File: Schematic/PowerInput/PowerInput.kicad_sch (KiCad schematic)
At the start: 25 parts, among them J101 PSU1 Pri, J102 PSU2 Pri, J103 PSU1 Sec, J104 PSU2 Sec, J105 Power LED, J106 230VAC In, J107 Power switch, J108 To MainBoard, J109 To Heater PSU

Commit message: Added filtering on PSU1 secondary
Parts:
- added C102: 220µF 35V, Capacitor_THT:CP_Radial_D10.0mm_P7.50mm, symbol Device:C_Polarized
- added FB101, FB102: FerriteBead, Inductor_SMD:L_1812_4532Metric_Pad1.30x3.40mm_HandSolder, symbol Device:FerriteBead
- added L101: 330µH 3.3A, Inductor_THT:L_Radial_D24.4mm_P23.70mm_Murata_1400series, symbol Device:L_Ferrite
- R102: value 1kΩ 1/2W -> 3.9kΩ 1/2W
- renumbered F102 to F101, F101 to F102, J108 to J104, J106 to J105, J105 to J106, J104 to J108
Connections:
- net Earth: now also J103.1 (Pin_1), J104.1 (Pin_1), C102.2; no longer J103.2 (Pin_2), J104.2 (Pin_2)
- net PSU1_19V: now also F101.2, J103.2 (Pin_2); no longer F101.1, J104.1 (Pin_1), R101.1, R102.1
- net PSU2_0V: now also FB102.1; no longer D102.1 (K), J109.2 (Pin_2)
- net PSU2_19V: now also F103.2, J108.1 (Pin_1); no longer F103.1, J109.1 (Pin_1), R103.1
- new net: F101.1, L101.2
- new net: F103.1, FB101.1
- new net HeaterPSU_0V: D102.1 (K), FB102.2, J109.2 (Pin_2)
- new net HeaterPSU_19V: FB101.2, J109.1 (Pin_1), R103.1
- new net MainBoard_19V: C102.1, J104.2 (Pin_2), L101.1, R101.1, R102.1
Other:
- moved on the sheet: D101, D102, F101, F103, J104, J106, J108, J109, R101, R102, R103

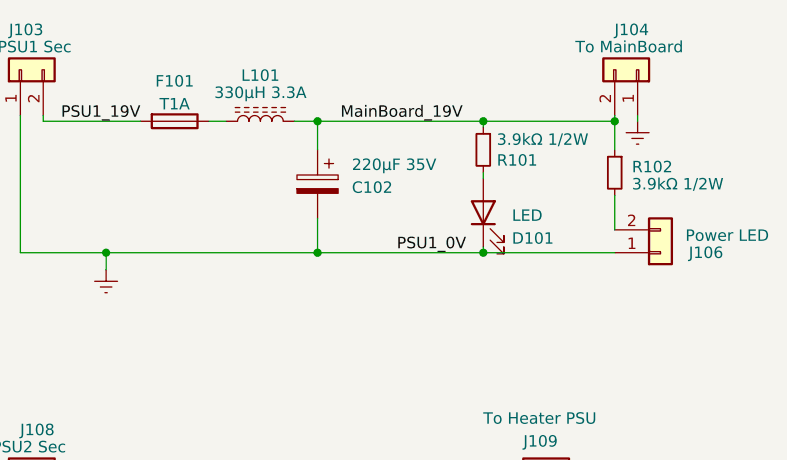
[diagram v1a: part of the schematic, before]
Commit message: Larger mounting hole for rotary switch
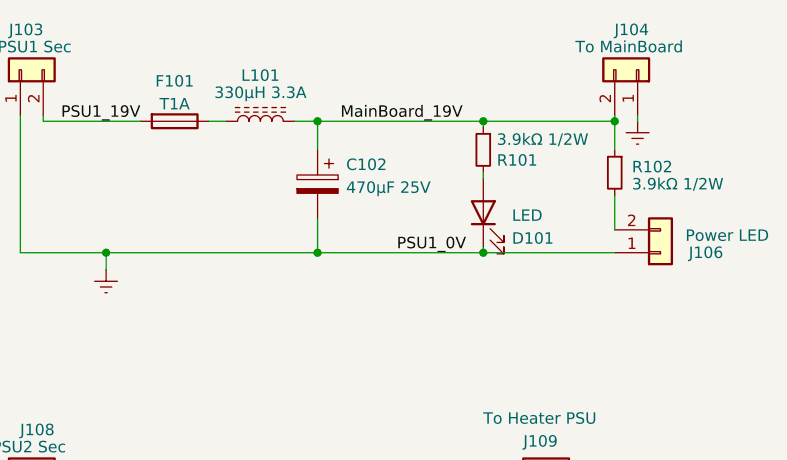
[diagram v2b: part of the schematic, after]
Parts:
- C102: value 220µF 35V -> 470µF 25V
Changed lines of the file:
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@@
   (symbol (lib_id "Device:C_Polarized") (at 172.085 74.93 0) (mirror y) (unit 1)
     (in_bom yes) (on_board yes) (fields_autoplaced)
-    (property "Reference" "C102" (id 0) (at 175.895 75.3111 0)
+    (property "Reference" "C102" (id 0) (at 175.26 72.7709 0)
       (effects (font (size 1.27 1.27)) (justify right))
     )
-    (property "Value" "220µF 35V" (id 1) (at 175.895 72.7711 0)
+    (property "Value" "470µF 25V" (id 1) (at 175.26 75.3109 0)
       (effects (font (size 1.27 1.27)) (justify right))
     )
@@
     )
     (path "/e68d4bfc-28fa-42c7-b027-c6bcd125d5f6"
-      (reference "C102") (unit 1) (value "220µF 35V") (footprint "Capacitor_THT:CP_Radial_D10.0mm_P7.50mm")
+      (reference "C102") (unit 1) (value "470µF 25V") (footprint "Capacitor_THT:CP_Radial_D10.0mm_P7.50mm")
     )
     (path "/089898c7-9db1-4682-8c8f-00decb94c3b6"

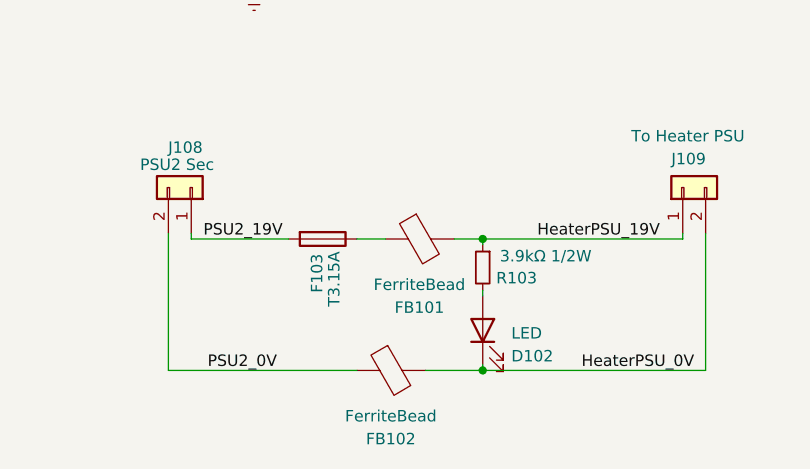
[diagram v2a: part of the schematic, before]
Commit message: Added BOM (bill of materials)
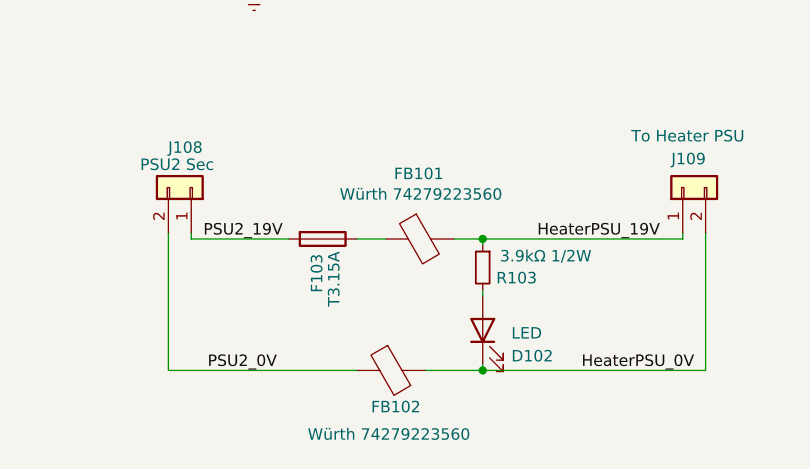
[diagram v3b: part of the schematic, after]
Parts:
- FB101, FB102: value FerriteBead -> Würth 74279223560
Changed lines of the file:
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@@
       (effects (font (size 1.27 1.27)) hide)
     )
-    (property "Datasheet" "~" (id 3) (at 113.03 62.23 0)
+    (property "Datasheet" "https://datasheet.lcsc.com/lcsc/2301061509_DIBO-DB128L-5-08-2P-BK-S_C430601.pdf" (id 3) (at 113.03 62.23 0)
       (effects (font (size 1.27 1.27)) hide)
     )
@@
       (effects (font (size 1.27 1.27)) hide)
     )
-    (property "Datasheet" "~" (id 3) (at 123.19 62.23 0)
+    (property "Datasheet" "https://datasheet.lcsc.com/lcsc/2301061509_DIBO-DB128L-5-08-2P-BK-S_C430601.pdf" (id 3) (at 123.19 62.23 0)
       (effects (font (size 1.27 1.27)) hide)
     )
@@
       (effects (font (size 1.27 1.27)) hide)
     )
-    (property "Datasheet" "~" (id 3) (at 141.605 106.68 0)
+    (property "Datasheet" "https://datasheet.lcsc.com/lcsc/2301061509_DIBO-DB128L-5-08-2P-BK-S_C430601.pdf" (id 3) (at 141.605 106.68 0)
       (effects (font (size 1.27 1.27)) hide)
     )
@@
   )
   (symbol (lib_id "Device:FerriteBead") (at 167.005 112.395 90) (mirror x) (unit 1)
-    (in_bom yes) (on_board yes) (fields_autoplaced)
-    (property "Reference" "FB101" (id 0) (at 166.9542 120.015 90))
-    (property "Value" "FerriteBead" (id 1) (at 166.9542 117.475 90))
+    (in_bom yes) (on_board yes)
+    (property "Reference" "FB101" (id 0) (at 166.878 105.156 90))
+    (property "Value" "Würth 74279223560" (id 1) (at 167.132 107.442 90))
     (property "Footprint" "Inductor_SMD:L_1812_4532Metric_Pad1.30x3.40mm_HandSolder" (id 2) (at 167.005 110.617 90)
       (effects (font (size 1.27 1.27)) hide)
@@
       (effects (font (size 1.27 1.27)) hide)
     )
-    (property "Datasheet" "~" (id 3) (at 139.065 62.23 0)
+    (property "Datasheet" "https://datasheet.lcsc.com/lcsc/2301061509_DIBO-DB128L-5-08-2P-BK-S_C430601.pdf" (id 3) (at 139.065 62.23 0)
       (effects (font (size 1.27 1.27)) hide)
     )
@@
       (effects (font (size 1.27 1.27)) hide)
     )
-    (property "Datasheet" "~" (id 3) (at 79.375 85.09 0)
+    (property "Datasheet" "https://datasheet.lcsc.com/lcsc/2301061509_DIBO-DB128L-5-08-2P-BK-S_C430601.pdf" (id 3) (at 79.375 85.09 0)
       (effects (font (size 1.27 1.27)) hide)
     )
@@
       (effects (font (size 1.27 1.27)) hide)
     )
-    (property "Datasheet" "~" (id 3) (at 210.185 82.55 0)
+    (property "Datasheet" "https://datasheet.lcsc.com/lcsc/2301061509_DIBO-DB128L-5-08-2P-BK-S_C430601.pdf" (id 3) (at 210.185 82.55 0)
       (effects (font (size 1.27 1.27)) hide)
     )
@@
   )
   (symbol (lib_id "Device:FerriteBead") (at 163.83 127 90) (mirror x) (unit 1)
-    (in_bom yes) (on_board yes) (fields_autoplaced)
-    (property "Reference" "FB102" (id 0) (at 163.7792 134.62 90))
-    (property "Value" "FerriteBead" (id 1) (at 163.7792 132.08 90))
+    (in_bom yes) (on_board yes)
+    (property "Reference" "FB102" (id 0) (at 164.338 131.064 90))
+    (property "Value" "Würth 74279223560" (id 1) (at 163.576 134.112 90))
     (property "Footprint" "Inductor_SMD:L_1812_4532Metric_Pad1.30x3.40mm_HandSolder" (id 2) (at 163.83 125.222 90)
       (effects (font (size 1.27 1.27)) hide)
@@
       (effects (font (size 1.27 1.27)) hide)
     )
-    (property "Datasheet" "~" (id 3) (at 59.69 77.47 0)
+    (property "Datasheet" "https://datasheet.lcsc.com/lcsc/2301061509_DIBO-DB128L-5-08-3P-BK-S_C430602.pdf" (id 3) (at 59.69 77.47 0)
       (effects (font (size 1.27 1.27)) hide)
     )
@@
       (effects (font (size 1.27 1.27)) hide)
     )
-    (property "Datasheet" "~" (id 3) (at 196.215 106.68 0)
+    (property "Datasheet" "https://datasheet.lcsc.com/lcsc/2301061509_DIBO-DB128L-5-08-2P-BK-S_C430601.pdf" (id 3) (at 196.215 106.68 0)
       (effects (font (size 1.27 1.27)) hide)
     )
@@
       (effects (font (size 1.27 1.27)) hide)
     )
-    (property "Datasheet" "~" (id 3) (at 207.645 62.23 0)
+    (property "Datasheet" "https://datasheet.lcsc.com/lcsc/2301061509_DIBO-DB128L-5-08-2P-BK-S_C430601.pdf" (id 3) (at 207.645 62.23 0)
       (effects (font (size 1.27 1.27)) hide)
     )
@@
     )
     (path "/65332850-1a77-474b-a20c-770d217595d9"
-      (reference "FB101") (unit 1) (value "FerriteBead") (footprint "Inductor_SMD:L_1812_4532Metric_Pad1.30x3.40mm_HandSolder")
+      (reference "FB101") (unit 1) (value "Würth 74279223560") (footprint "Inductor_SMD:L_1812_4532Metric_Pad1.30x3.40mm_HandSolder")
     )
     (path "/cadfc194-56aa-4a1e-a1ef-41d398cc2835"
-      (reference "FB102") (unit 1) (value "FerriteBead") (footprint "Inductor_SMD:L_1812_4532Metric_Pad1.30x3.40mm_HandSolder")
+      (reference "FB102") (unit 1) (value "Würth 74279223560") (footprint "Inductor_SMD:L_1812_4532Metric_Pad1.30x3.40mm_HandSolder")
     )
     (path "/11df9c08-382c-456e-87de-e48da6c6525a"
